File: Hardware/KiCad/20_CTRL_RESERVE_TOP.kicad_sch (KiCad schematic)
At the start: 0 parts

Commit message: hardware: detail 20 control reserve top sheet
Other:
- note added: "20_CTRL_RESERVE_TOP - PCB-B_CTRL_RESERVE Purpose: define control, critical power, EMG and communication functional zones. High-current load power must not pass through PCB-B."
- note added: "COMMUNICATIONS Isolated RS-485 is the active external communication interface. Optional CAN/CAN-FD footprints may remain DNP only. ISO_GND remains separate from POWER_GND/SIGNAL_GND until EMC decision."
- note added: "CONTROL OUTPUTS To PCB-A: MAIN_SWx, BALANCE_SWx, hold-loop open, discharge, EXT_KILL chain. To PCB-C/D/E: channel enables, group safe-off, PWM and reset lines. Parallel vs serialized control remains TBD."
- note added: "CRITICAL POWER / EMG PACK_BUS_CRIT_IN feeds reserve/critical power only. EMG / KEEP_ALIVE sustains MCU logging and controlled shutdown. EMG must not power heavy external loads."
- note added: "DIAGNOSTIC INPUTS From PCB-A: battery/pack measurements and BFE faults. From PCB-C/D/E: channel current, voltage, fault, status and temperatures. Muxed analog, SPI/I2C or parallel topology remains TBD."
- note added: "GROUND / SAFETY RULES POWER_GND, SIGNAL_GND, ISO_GND and CHASSIS are not automatically shorted. EXT_KILL input must propagate to final actuators without depending on MCU code. Critical power must support orderly logging after HARD_OFF."
- note added: "MCU / FAULT MANAGER MCU supervises normal control, diagnostics and logging. Watchdog/supervisor provides reset and fault containment. Safety-critical EXT_KILL path has hardware priority over firmware."
- note added: "SERVICE / DEBUG SWD/debug and service UART are internal/service only. Debug access must not bypass EXT_KILL/HARD_OFF. Boot/config straps and programming connector family are TBD."
- note removed: "PCB-B_CTRL_RESERVE CONTAINS: MCU, watchdog/supervisor, EMG/KEEP_ALIVE, RESERVE_BRANCH, 5V_CRIT, 3V3_CRIT, isolated RS-485, optional CAN footprint DNP, service/debug, control and diagnostic IO."
- note removed: "POWER RULES: Receives PACK_BUS_CRIT_IN only for critical/EMG path. Does not carry summed CH1..CH14 current, 5V_SYS current, LED current, or BAT1/BAT2 main power. 5V_CRIT and 3V3_CRIT do not power external outputs."
- note removed: "SAFETY/CONTROL: EXT_KILL input must generate hardware final actions on PCB-A independent of MCU. MCU may log and supervise but must not be the only path for HARD_OFF. All interboard signals follow Docs/INTERBOARD_INTERFACES.md and NET_NAMING_RULES.md."
- company: (none) -> Gonoboben/plataVM
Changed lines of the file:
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@@
 	(title_block
 		(title "20_CTRL_RESERVE_TOP - PCB-B_CTRL_RESERVE")
-		(date "2026-07-14")
-		(rev "A0")
-		(comment 1 "MCU, EMG, critical power, supervisor, RS-485, control IO")
+		(date "2026-07-15")
+		(rev "A1")
+		(company "Gonoboben/plataVM")
+		(comment 1 "Architecture Level A: MCU, critical power, EMG, RS-485, control IO")
+		(comment 2 "No MCU/DC-DC/transceiver part numbers selected")
 	)
-	(text "PCB-B_CTRL_RESERVE CONTAINS:\nMCU, watchdog/supervisor, EMG/KEEP_ALIVE, RESERVE_BRANCH, 5V_CRIT, 3V3_CRIT, isolated RS-485, optional CAN footprint DNP, service/debug, control and diagnostic IO."
+	(text "20_CTRL_RESERVE_TOP - PCB-B_CTRL_RESERVE\nPurpose: define control, critical power, EMG and communication functional zones.\nHigh-current load power must not pass through PCB-B."
 		(exclude_from_sim no)
-		(at 20 25 0)
-		(effects
-			(font
-				(size 1.8 1.8)
-			)
-			(justify left)
-		)
+		(at 12 10 0)
+		(effects (font (size 1.55 1.55)) (justify left))
+		(uuid "ctrl-b-text-0001")
 	)
-	(text "SAFETY/CONTROL:\nEXT_KILL input must generate hardware final actions on PCB-A independent of MCU.\nMCU may log and supervise but must not be the only path for HARD_OFF.\nAll interboard signals follow Docs/INTERBOARD_INTERFACES.md and NET_NAMING_RULES.md."
+	(text "CRITICAL POWER / EMG\nPACK_BUS_CRIT_IN feeds reserve/critical power only.\nEMG / KEEP_ALIVE sustains MCU logging and controlled shutdown.\nEMG must not power heavy external loads."
 		(exclude_from_sim no)
-		(at 20 135 0)
-		(effects
-			(font
-				(size 1.8 1.8)
-			)
-			(justify left)
-		)
+		(at 12 38 0)
+		(effects (font (size 1.3 1.3)) (justify left))
+		(uuid "ctrl-b-text-0002")
 	)
-	(text "POWER RULES:\nReceives PACK_BUS_CRIT_IN only for critical/EMG path.\nDoes not carry summed CH1..CH14 current, 5V_SYS current, LED current, or BAT1/BAT2 main power.\n5V_CRIT and 3V3_CRIT do not power external outputs."
+	(text "MCU / FAULT MANAGER\nMCU supervises normal control, diagnostics and logging.\nWatchdog/supervisor provides reset and fault containment.\nSafety-critical EXT_KILL path has hardware priority over firmware."
 		(exclude_from_sim no)
-		(at 20 75 0)
-		(effects
-			(font
-				(size 1.8 1.8)
-			)
-			(justify left)
-		)
+		(at 112 38 0)
+		(effects (font (size 1.3 1.3)) (justify left))
+		(uuid "ctrl-b-text-0003")
 	)
+	(text "COMMUNICATIONS\nIsolated RS-485 is the active external communication interface.\nOptional CAN/CAN-FD footprints may remain DNP only.\nISO_GND remains separate from POWER_GND/SIGNAL_GND until EMC decision."
+		(exclude_from_sim no)
+		(at 222 38 0)
+		(effects (font (size 1.3 1.3)) (justify left))
+		(uuid "ctrl-b-text-0004")
+	)
+	(text "CONTROL OUTPUTS\nTo PCB-A: MAIN_SWx, BALANCE_SWx, hold-loop open, discharge, EXT_KILL chain.\nTo PCB-C/D/E: channel enables, group safe-off, PWM and reset lines.\nParallel vs serialized control remains TBD."
+		(exclude_from_sim no)
+		(at 12 112 0)
+		(effects (font (size 1.3 1.3)) (justify left))
+		(uuid "ctrl-b-text-0005")
+	)
+	(text "DIAGNOSTIC INPUTS\nFrom PCB-A: battery/pack measurements and BFE faults.\nFrom PCB-C/D/E: channel current, voltage, fault, status and temperatures.\nMuxed analog, SPI/I2C or parallel topology remains TBD."
+		(exclude_from_sim no)
+		(at 112 112 0)
+		(effects (font (size 1.3 1.3)) (justify left))
+		(uuid "ctrl-b-text-0006")
+	)
+	(text "SERVICE / DEBUG\nSWD/debug and service UART are internal/service only.\nDebug access must not bypass EXT_KILL/HARD_OFF.\nBoot/config straps and programming connector family are TBD."
+		(exclude_from_sim no)
+		(at 222 112 0)
+		(effects (font (size 1.3 1.3)) (justify left))
+		(uuid "ctrl-b-text-0007")
+	)
+	(text "GROUND / SAFETY RULES\nPOWER_GND, SIGNAL_GND, ISO_GND and CHASSIS are not automatically shorted.\nEXT_KILL input must propagate to final actuators without depending on MCU code.\nCritical power must support orderly logging after HARD_OFF."
+		(exclude_from_sim no)
+		(at 12 190 0)
+		(effects (font (size 1.25 1.25)) (justify left))
+		(uuid "ctrl-b-text-0008")
+	)
+	(hierarchical_label "PACK_BUS_CRIT_IN" (shape passive) (exclude_from_sim no) (at 68 62 0) (effects (font (size 1.15 1.15)) (justify left)) (uuid "ctrl-b-label-0001"))
+	(hierarchical_label "5V_CRIT" (shape passive) (exclude_from_sim no) (at 68 70 0) (effects (font (size 1.15 1.15)) (justify left)) (uuid "ctrl-b-label-0002"))
+	(hierarchical_label "3V3_CRIT" (shape passive) (exclude_from_sim no) (at 68 78 0) (effects (font (size 1.15 1.15)) (justify left)) (uuid "ctrl-b-label-0003"))
+	(hierarchical_label "MCU_FAULT_MANAGER" (shape passive) (exclude_from_sim no) (at 166 66 0) (effects (font (size 1.15 1.15)) (justify left)) (uuid "ctrl-b-label-0004"))
+	(hierarchical_label "RS485_ISOLATED" (shape passive) (exclude_from_sim no) (at 270 66 0) (effects (font (size 1.15 1.15)) (justify left)) (uuid "ctrl-b-label-0005"))
+	(hierarchical_label "ISO_GND_POLICY" (shape passive) (exclude_from_sim no) (at 270 74 0) (effects (font (size 1.15 1.15)) (justify left)) (uuid "ctrl-b-label-0006"))
+	(hierarchical_label "CTRL_B_TO_A" (shape passive) (exclude_from_sim no) (at 70 146 0) (effects (font (size 1.15 1.15)) (justify left)) (uuid "ctrl-b-label-0007"))
+	(hierarchical_label "CTRL_B_TO_C_P12" (shape passive) (exclude_from_sim no) (at 70 154 0) (effects (font (size 1.15 1.15)) (justify left)) (uuid "ctrl-b-label-0008"))
+	(hierarchical_label "CTRL_B_TO_D_P5" (shape passive) (exclude_from_sim no) (at 70 162 0) (effects (font (size 1.15 1.15)) (justify left)) (uuid "ctrl-b-label-0009"))
+	(hierarchical_label "CTRL_B_TO_E_LIGHT" (shape passive) (exclude_from_sim no) (at 70 170 0) (effects (font (size 1.15 1.15)) (justify left)) (uuid "ctrl-b-label-0010"))
+	(hierarchical_label "DIAG_A_TO_B" (shape passive) (exclude_from_sim no) (at 170 146 0) (effects (font (size 1.15 1.15)) (justify left)) (uuid "ctrl-b-label-0011"))
+	(hierarchical_label "DIAG_C_TO_B_P12" (shape passive) (exclude_from_sim no) (at 170 154 0) (effects (font (size 1.15 1.15)) (justify left)) (uuid "ctrl-b-label-0012"))
+	(hierarchical_label "DIAG_D_TO_B_P5" (shape passive) (exclude_from_sim no) (at 170 162 0) (effects (font (size 1.15 1.15)) (justify left)) (uuid "ctrl-b-label-0013"))
+	(hierarchical_label "DIAG_E_TO_B_LIGHT" (shape passive) (exclude_from_sim no) (at 170 170 0) (effects (font (size 1.15 1.15)) (justify left)) (uuid "ctrl-b-label-0014"))
+	(hierarchical_label "EXT_KILL_HW_CHAIN" (shape passive) (exclude_from_sim no) (at 12 230 0) (effects (font (size 1.15 1.15)) (justify left)) (uuid "ctrl-b-label-0015"))
+	(hierarchical_label "SERVICE_DEBUG" (shape passive) (exclude_from_sim no) (at 270 146 0) (effects (font (size 1.15 1.15)) (justify left)) (uuid "ctrl-b-label-0016"))
 )

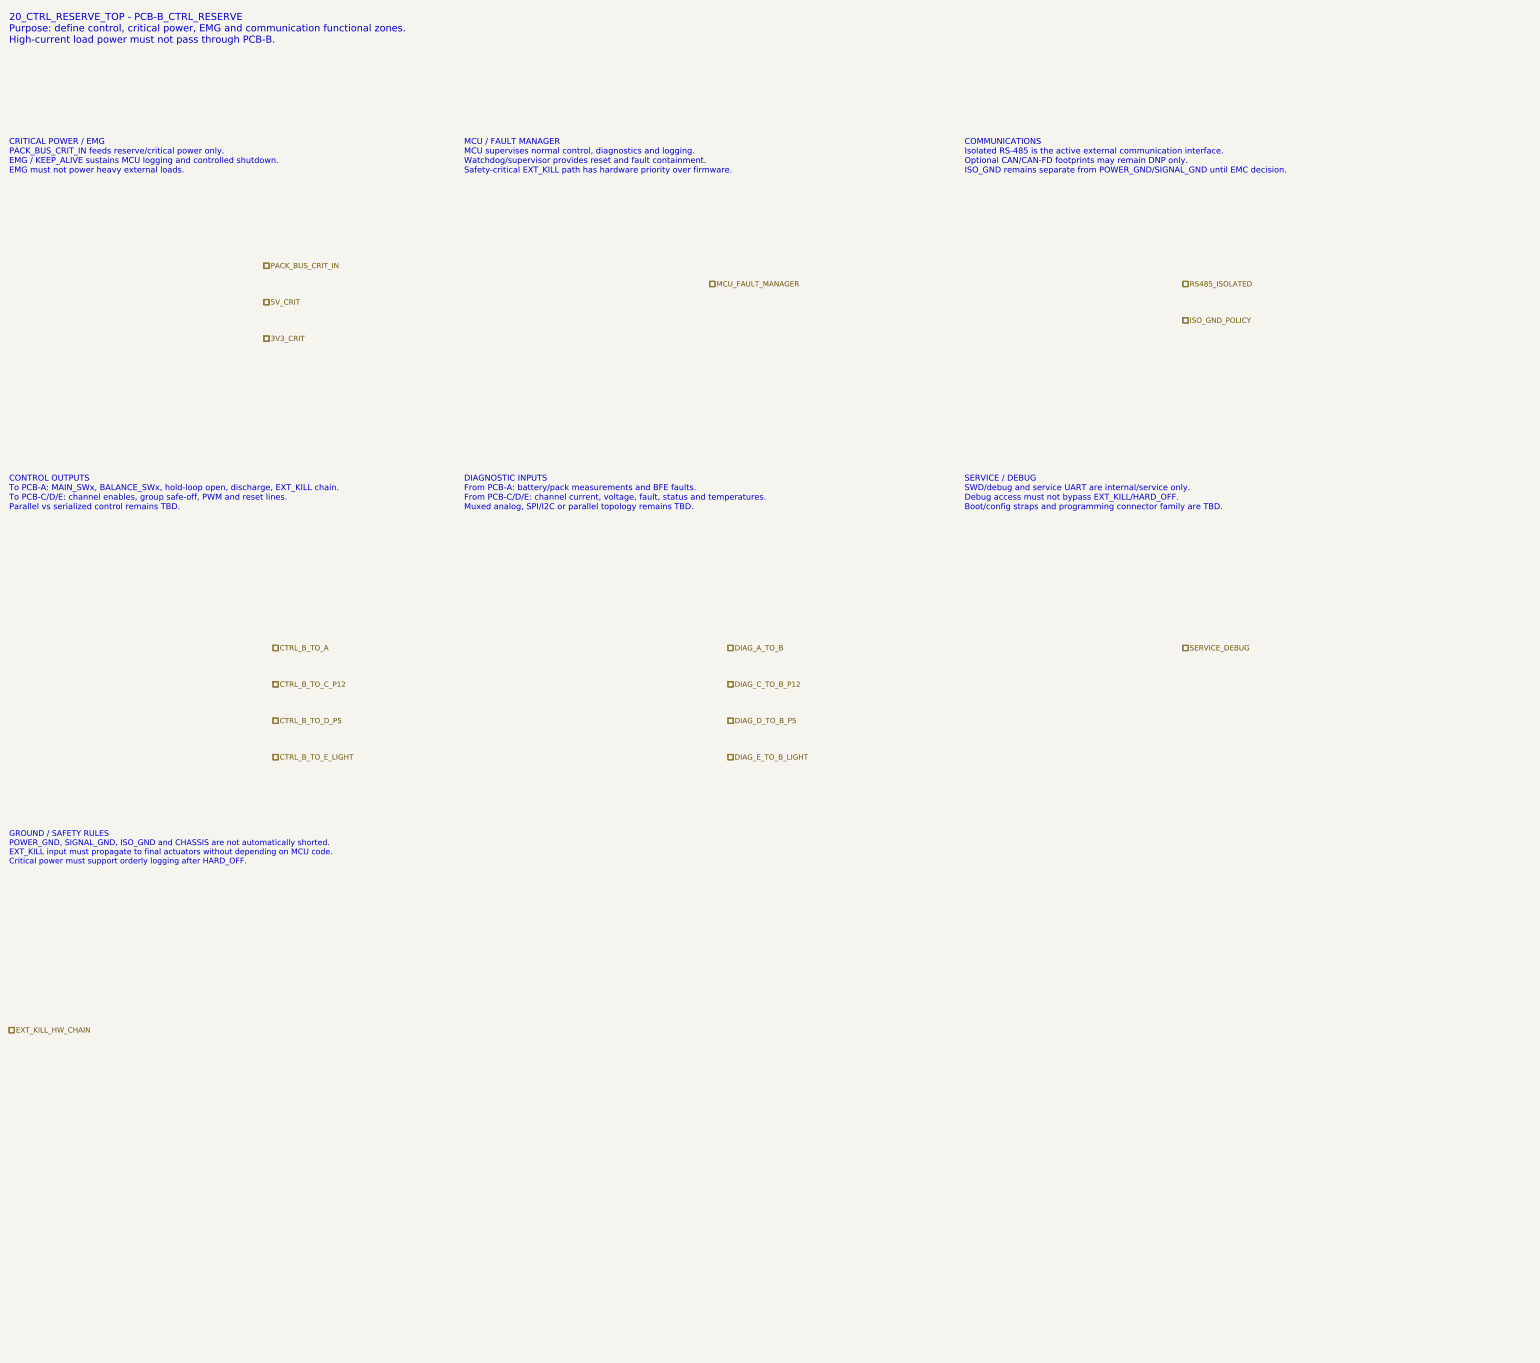
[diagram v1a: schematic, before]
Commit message: hardware: add PCB-B CTRL_RESERVE detailed hierarchy
Merge PCB-B Architecture Level A/B hierarchy after confirming preserved interfaces and safety constraints.
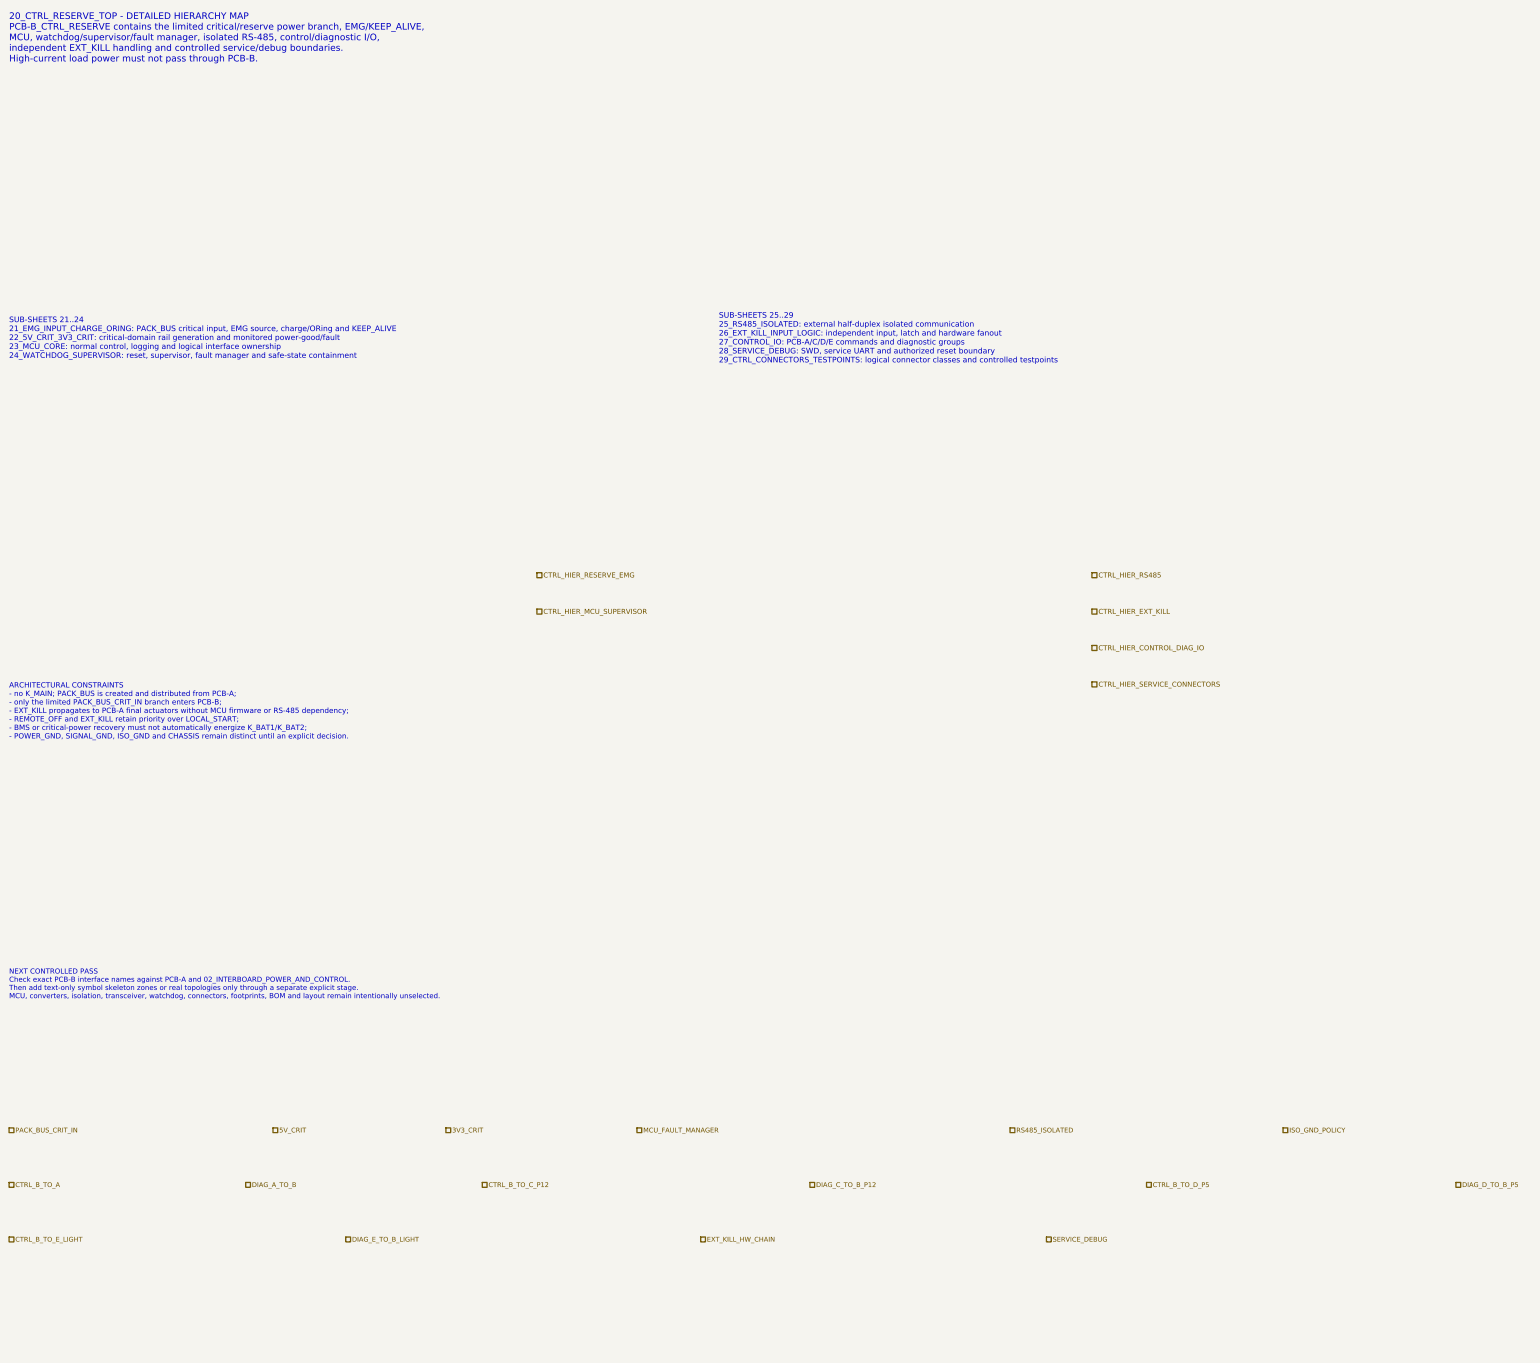
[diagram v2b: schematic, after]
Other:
- note added: "20_CTRL_RESERVE_TOP - DETAILED HIERARCHY MAP PCB-B_CTRL_RESERVE contains the limited critical/reserve power branch, EMG/KEEP_ALIVE, MCU, watchdog/supervisor/fault manager, isolated RS-485, control/diagnostic I/O, independent EXT_KILL handling and controlled service/debug boundaries. High-current load power must not pass through PCB-B."
- note added: "ARCHITECTURAL CONSTRAINTS - no K_MAIN; PACK_BUS is created and distributed from PCB-A; - only the limited PACK_BUS_CRIT_IN branch enters PCB-B; - EXT_KILL propagates to PCB-A final actuators without MCU firmware or RS-485 dependency; - REMOTE_OFF and EXT_KILL retain priority over LOCAL_START; - BMS or critical-power recovery must not automatically energize K_BAT1/K_BAT2; - POWER_GND, SIGNAL_GND, 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"
- note added: "NEXT CONTROLLED PASS Check exact PCB-B interface names against PCB-A and 02_INTERBOARD_POWER_AND_CONTROL. Then add text-only symbol skeleton zones or real topologies only through a separate explicit stage. MCU, converters, isolation, transceiver, watchdog, connectors, footprints, BOM and layout remain intentionally unselected."
- note added: "SUB-SHEETS 21..24 21_EMG_INPUT_CHARGE_ORING: PACK_BUS critical input, EMG source, charge/ORing and KEEP_ALIVE 22_5V_CRIT_3V3_CRIT: critical-domain rail generation and monitored power-good/fault 23_MCU_CORE: normal control, logging and logical interface ownership 24_WATCHDOG_SUPERVISOR: reset, supervisor, fault manager and safe-state containment"
- note added: "SUB-SHEETS 25..29 25_RS485_ISOLATED: external half-duplex isolated communication 26_EXT_KILL_INPUT_LOGIC: independent input, latch and hardware fanout 27_CONTROL_IO: PCB-A/C/D/E commands and diagnostic groups 28_SERVICE_DEBUG: SWD, service UART and authorized reset boundary 29_CTRL_CONNECTORS_TESTPOINTS: logical connector classes and controlled testpoints"
- note removed: "20_CTRL_RESERVE_TOP - PCB-B_CTRL_RESERVE Purpose: define control, critical power, EMG and communication functional zones. High-current load power must not pass through PCB-B."
- note removed: "COMMUNICATIONS Isolated RS-485 is the active external communication interface. Optional CAN/CAN-FD footprints may remain DNP only. ISO_GND remains separate from POWER_GND/SIGNAL_GND until EMC decision."
- note removed: "CONTROL OUTPUTS To PCB-A: MAIN_SWx, BALANCE_SWx, hold-loop open, discharge, EXT_KILL chain. To PCB-C/D/E: channel enables, group safe-off, PWM and reset lines. Parallel vs serialized control remains TBD."
- note removed: "CRITICAL POWER / EMG PACK_BUS_CRIT_IN feeds reserve/critical power only. EMG / KEEP_ALIVE sustains MCU logging and controlled shutdown. EMG must not power heavy external loads."
- note removed: "DIAGNOSTIC INPUTS From PCB-A: battery/pack measurements and BFE faults. From PCB-C/D/E: channel current, voltage, fault, status and temperatures. Muxed analog, SPI/I2C or parallel topology remains TBD."
- note removed: "GROUND / SAFETY RULES POWER_GND, SIGNAL_GND, ISO_GND and CHASSIS are not automatically shorted. EXT_KILL input must propagate to final actuators without depending on MCU code. Critical power must support orderly logging after HARD_OFF."
- note removed: "MCU / FAULT MANAGER MCU supervises normal control, diagnostics and logging. Watchdog/supervisor provides reset and fault containment. Safety-critical EXT_KILL path has hardware priority over firmware."
- note removed: "SERVICE / DEBUG SWD/debug and service UART are internal/service only. Debug access must not bypass EXT_KILL/HARD_OFF. Boot/config straps and programming connector family are TBD."
